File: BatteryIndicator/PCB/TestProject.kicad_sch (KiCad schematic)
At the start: 6 parts, among them J1_XT60 Conn_01x02_Male, J2_Buck1 Conn_01x03_Female, J3_MCU_Left1 Conn_01x07_Female, J3_MCU_Right1 Conn_01x07_Female, J4_LED1 Conn_01x03_Male, J5_Button1 Conn_01x02_Male

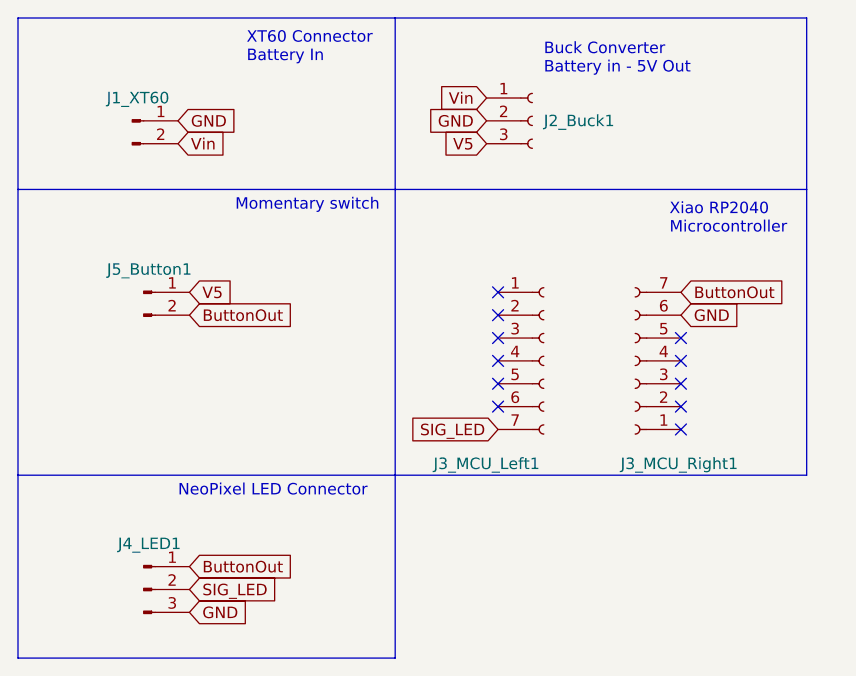
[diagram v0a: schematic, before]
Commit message: Added UART pins to PCB
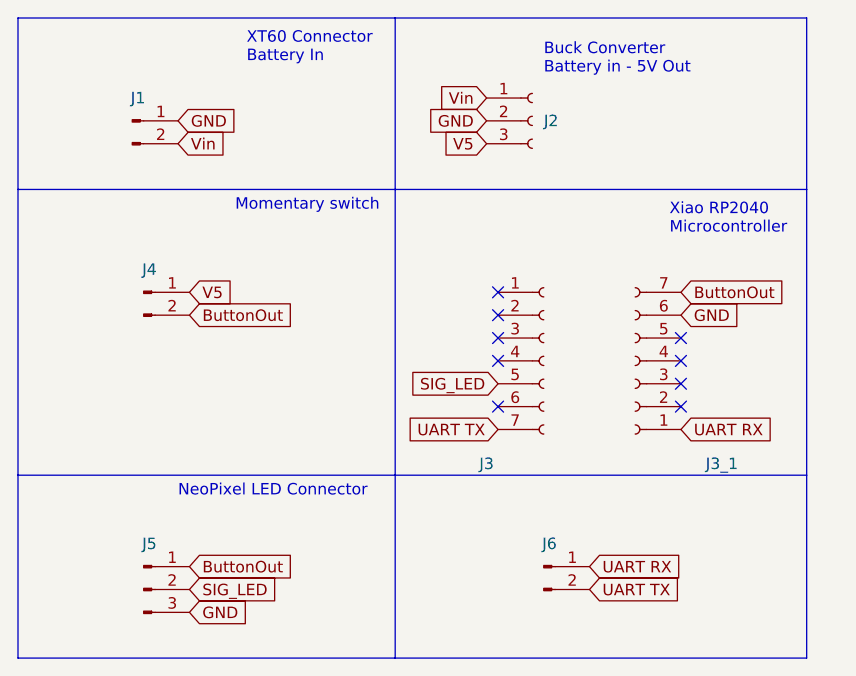
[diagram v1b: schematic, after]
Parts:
- added J6: Conn_01x02_Male, Connector_PinHeader_2.54mm:PinHeader_1x02_P2.54mm_Vertical, symbol Connector:Conn_01x02_Male
- J5: renamed from J4_LED1; footprint (none) -> Connector_PinHeader_2.54mm:PinHeader_1x03_P2.54mm_Vertical
- renumbered J1_XT60 to J1, J2_Buck1 to J2, J3_MCU_Left1 to J3, J3_MCU_Right1 to J3_1, J5_Button1 to J4
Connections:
- net SIG_LED: now also J3.5 (Pin_5); no longer J3.7 (Pin_7)
- net UART RX: now reaches J3_1.1 (Pin_1)
- net UART RX: now also J6.1 (Pin_1)
- new net UART TX: J3.7 (Pin_7), J6.2 (Pin_2)
- no-connect marks 11 -> 9
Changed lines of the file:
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@@
   (no_connect (at 66.04 50.8))
   (no_connect (at 66.04 48.26))
-  (no_connect (at 66.04 53.34))
-  (no_connect (at 86.36 58.42))
   (no_connect (at 86.36 53.34))
   (no_connect (at 86.36 48.26))
   (no_connect (at 86.36 50.8))
+  (polyline (pts (xy 100.33 63.5) (xy 100.33 83.82))
+    (stroke (width 0) (type default) (color 0 0 0 0))
+  )
   (polyline (pts (xy 54.61 63.5) (xy 100.33 63.5))
     (stroke (width 0) (type default) (color 0 0 0 0))
@@
     (stroke (width 0) (type default) (color 0 0 0 0))
   )
+  (polyline (pts (xy 54.61 83.82) (xy 100.33 83.82))
+    (stroke (width 0) (type default) (color 0 0 0 0))
+  )
   (polyline (pts (xy 100.33 12.7) (xy 54.61 12.7))
     (stroke (width 0) (type default) (color 0 0 0 0))
@@
     )
   )
+  (global_label "UART RX" (shape input) (at 86.36 58.42 0) (fields_autoplaced)
+    (effects (font (size 1.27 1.27)) (justify left))
+    (property "Intersheet References" "${INTERSHEET_REFS}" (id 0) (at 96.8769 58.3406 0)
+      (effects (font (size 1.27 1.27)) (justify left) hide)
+    )
+  )
   (global_label "Vin" (shape input) (at 64.77 21.59 180) (fields_autoplaced)
     (effects (font (size 1.27 1.27)) (justify right))
@@
     )
   )
+  (global_label "UART TX" (shape input) (at 66.04 58.42 180) (fields_autoplaced)
+    (effects (font (size 1.27 1.27)) (justify right))
+    (property "Intersheet References" "${INTERSHEET_REFS}" (id 0) (at 55.8255 58.4994 0)
+      (effects (font (size 1.27 1.27)) (justify right) hide)
+    )
+  )
   (global_label "GND" (shape input) (at 31.75 78.74 0) (fields_autoplaced)
     (effects (font (size 1.27 1.27)) (justify left))
@@
     )
   )
+  (global_label "UART RX" (shape input) (at 76.2 73.66 0) (fields_autoplaced)
+    (effects (font (size 1.27 1.27)) (justify left))
+    (property "Intersheet References" "${INTERSHEET_REFS}" (id 0) (at 86.7169 73.5806 0)
+      (effects (font (size 1.27 1.27)) (justify left) hide)
+    )
+  )
   (global_label "SIG_LED" (shape input) (at 31.75 76.2 0) (fields_autoplaced)
     (effects (font (size 1.27 1.27)) (justify left))
@@
     )
   )
+  (global_label "UART TX" (shape input) (at 76.2 76.2 0) (fields_autoplaced)
+    (effects (font (size 1.27 1.27)) (justify left))
+    (property "Intersheet References" "${INTERSHEET_REFS}" (id 0) (at 86.4145 76.1206 0)
+      (effects (font (size 1.27 1.27)) (justify left) hide)
+    )
+  )
   (global_label "V5" (shape input) (at 31.75 43.18 0) (fields_autoplaced)
     (effects (font (size 1.27 1.27)) (justify left))
@@
     )
   )
-  (global_label "SIG_LED" (shape input) (at 66.04 58.42 180) (fields_autoplaced)
-    (effects (font (size 1.27 1.27)) (justify right))
-    (property "Intersheet References" "${INTERSHEET_REFS}" (id 0) (at 56.1279 58.4994 0)
+  (global_label "SIG_LED" (shape input) (at 66.04 53.34 180) (fields_autoplaced)
+    (effects (font (size 1.27 1.27)) (justify right))
+    (property "Intersheet References" "${INTERSHEET_REFS}" (id 0) (at 56.1279 53.4194 0)
       (effects (font (size 1.27 1.27)) (justify right) hide)
     )
@@
   (symbol (lib_id "Connector:Conn_01x02_Male") (at 26.67 43.18 0) (unit 1)
     (in_bom yes) (on_board yes) (fields_autoplaced)
-    (property "Reference" "J5_Button1" (id 0) (at 27.305 40.64 0))
+    (property "Reference" "J4" (id 0) (at 27.305 40.64 0))
     (property "Value" "Conn_01x02_Male" (id 1) (at 27.305 40.64 0)
       (effects (font (size 1.27 1.27)) hide)
@@
   (symbol (lib_id "Connector:Conn_01x03_Female") (at 69.85 24.13 0) (unit 1)
     (in_bom yes) (on_board yes) (fields_autoplaced)
-    (property "Reference" "J2_Buck1" (id 0) (at 71.12 24.1299 0)
+    (property "Reference" "J2" (id 0) (at 71.12 24.1299 0)
       (effects (font (size 1.27 1.27)) (justify left))
     )
@@
     (pin "2")
     (pin "3")
+  )
+  (symbol (lib_id "Connector:Conn_01x02_Male") (at 71.12 73.66 0) (unit 1)
+    (in_bom yes) (on_board yes) (fields_autoplaced)
+    (property "Reference" "J6" (id 0) (at 71.755 71.12 0))
+    (property "Value" "Conn_01x02_Male" (id 1) (at 71.755 71.12 0)
+      (effects (font (size 1.27 1.27)) hide)
+    )
+    (property "Footprint" "Connector_PinHeader_2.54mm:PinHeader_1x02_P2.54mm_Vertical" (id 2) (at 71.12 73.66 0)
+      (effects (font (size 1.27 1.27)) hide)
+    )
+    (property "Datasheet" "~" (id 3) (at 71.12 73.66 0)
+      (effects (font (size 1.27 1.27)) hide)
+    )
+    (pin "1")
+    (pin "2")
   )
   (symbol (lib_id "Connector:Conn_01x07_Female") (at 81.28 50.8 180) (unit 1)
     (in_bom yes) (on_board yes)
-    (property "Reference" "J3_MCU_Right1" (id 0) (at 92.71 62.23 0)
+    (property "Reference" "J3_1" (id 0) (at 92.71 62.23 0)
       (effects (font (size 1.27 1.27)) (justify left))
     )
@@
   (symbol (lib_id "Connector:Conn_01x07_Female") (at 71.12 50.8 0) (unit 1)
     (in_bom yes) (on_board yes)
-    (property "Reference" "J3_MCU_Left1" (id 0) (at 64.77 62.23 0))
+    (property "Reference" "J3" (id 0) (at 64.77 62.23 0))
     (property "Value" "Conn_01x07_Female" (id 1) (at 70.485 60.96 0)
       (effects (font (size 1.27 1.27)) hide)
@@
   (symbol (lib_id "Connector:Conn_01x03_Male") (at 26.67 76.2 0) (unit 1)
     (in_bom yes) (on_board yes) (fields_autoplaced)
-    (property "Reference" "J4_LED1" (id 0) (at 27.305 71.12 0))
+    (property "Reference" "J5" (id 0) (at 27.305 71.12 0))
     (property "Value" "Conn_01x03_Male" (id 1) (at 27.305 71.12 0)
       (effects (font (size 1.27 1.27)) hide)
     )
-    (property "Footprint" "" (id 2) (at 26.67 76.2 0)
+    (property "Footprint" "Connector_PinHeader_2.54mm:PinHeader_1x03_P2.54mm_Vertical" (id 2) (at 26.67 76.2 0)
       (effects (font (size 1.27 1.27)) hide)
     )
@@
   (symbol (lib_id "Connector:Conn_01x02_Male") (at 25.4 24.13 0) (unit 1)
     (in_bom yes) (on_board yes) (fields_autoplaced)
-    (property "Reference" "J1_XT60" (id 0) (at 26.035 21.59 0))
+    (property "Reference" "J1" (id 0) (at 26.035 21.59 0))
     (property "Value" "Conn_01x02_Male" (id 1) (at 26.035 21.59 0)
       (effects (font (size 1.27 1.27)) hide)
@@
   (symbol_instances
     (path "/eca73914-6f4b-487c-b8f6-6bedca0fa3fb"
-      (reference "J1_XT60") (unit 1) (value "Conn_01x02_Male") (footprint "Connector_AMASS:AMASS_XT60-M_1x02_P7.20mm_Vertical")
+      (reference "J1") (unit 1) (value "Conn_01x02_Male") (footprint "Connector_AMASS:AMASS_XT60-M_1x02_P7.20mm_Vertical")
     )
     (path "/3632fdce-08c8-42e5-b9d6-4604f78cc098"
-      (reference "J2_Buck1") (unit 1) (value "Conn_01x03_Female") (footprint "Connector_PinSocket_2.54mm:PinSocket_1x03_P2.54mm_Vertical")
+      (reference "J2") (unit 1) (value "Conn_01x03_Female") (footprint "Connector_PinSocket_2.54mm:PinSocket_1x03_P2.54mm_Vertical")
     )
     (path "/8cb0adaa-acd2-4046-aef3-2e8849a59b9f"
-      (reference "J3_MCU_Left1") (unit 1) (value "Conn_01x07_Female") (footprint "Connector_PinSocket_2.54mm:PinSocket_1x07_P2.54mm_Vertical")
+      (reference "J3") (unit 1) (value "Conn_01x07_Female") (footprint "Connector_PinSocket_2.54mm:PinSocket_1x07_P2.54mm_Vertical")
     )
     (path "/7981c0ba-a5a0-4ab9-a2ee-681c264b45da"
-      (reference "J3_MCU_Right1") (unit 1) (value "Conn_01x07_Female") (footprint "Connector_PinSocket_2.54mm:PinSocket_1x07_P2.54mm_Vertical")
+      (reference "J3_1") (unit 1) (value "Conn_01x07_Female") (footprint "Connector_PinSocket_2.54mm:PinSocket_1x07_P2.54mm_Vertical")
+    )
+    (path "/222a1c0d-2693-4802-ada8-5b0adcf96f0c"
+      (reference "J4") (unit 1) (value "Conn_01x02_Male") (footprint "Connector_PinHeader_2.54mm:PinHeader_1x02_P2.54mm_Vertical")
     )
     (path "/c11ca3bc-a8bb-430a-9e10-289b52cce878"
-      (reference "J4_LED1") (unit 1) (value "Conn_01x03_Male") (footprint "Connector_PinHeader_2.54mm:PinHeader_1x03_P2.54mm_Vertical")
-    )
-    (path "/222a1c0d-2693-4802-ada8-5b0adcf96f0c"
-      (reference "J5_Button1") (unit 1) (value "Conn_01x02_Male") (footprint "Connector_PinHeader_2.54mm:PinHeader_1x02_P2.54mm_Vertical")
-    )
-  )
+      (reference "J5") (unit 1) (value "Conn_01x03_Male") (footprint "Connector_PinHeader_2.54mm:PinHeader_1x03_P2.54mm_Vertical")
+    )
+    (path "/6150c02b-beb5-4af1-951e-3666a285a6ea"
+      (reference "J6") (unit 1) (value "Conn_01x02_Male") (footprint "Connector_PinHeader_2.54mm:PinHeader_1x02_P2.54mm_Vertical")
+    )
+  )
